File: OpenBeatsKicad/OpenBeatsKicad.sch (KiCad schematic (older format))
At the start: 30 parts

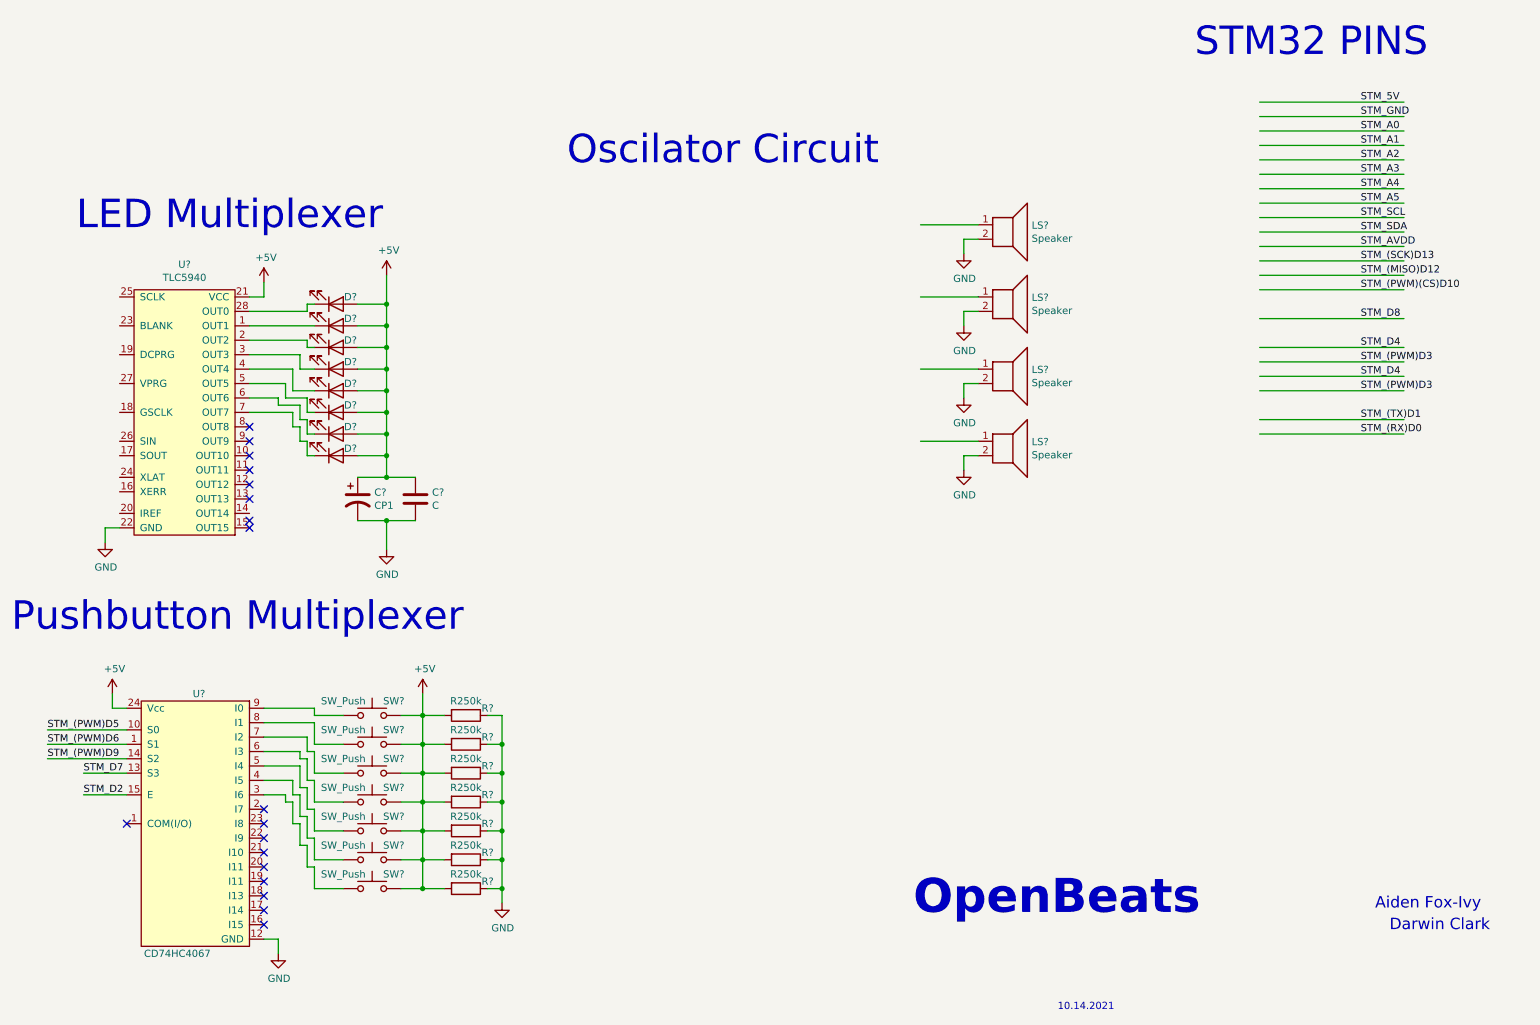
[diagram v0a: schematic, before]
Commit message: :sparkles: Connected all STM Pins, Finished Oscilator, and fixed naming conventions for passive components
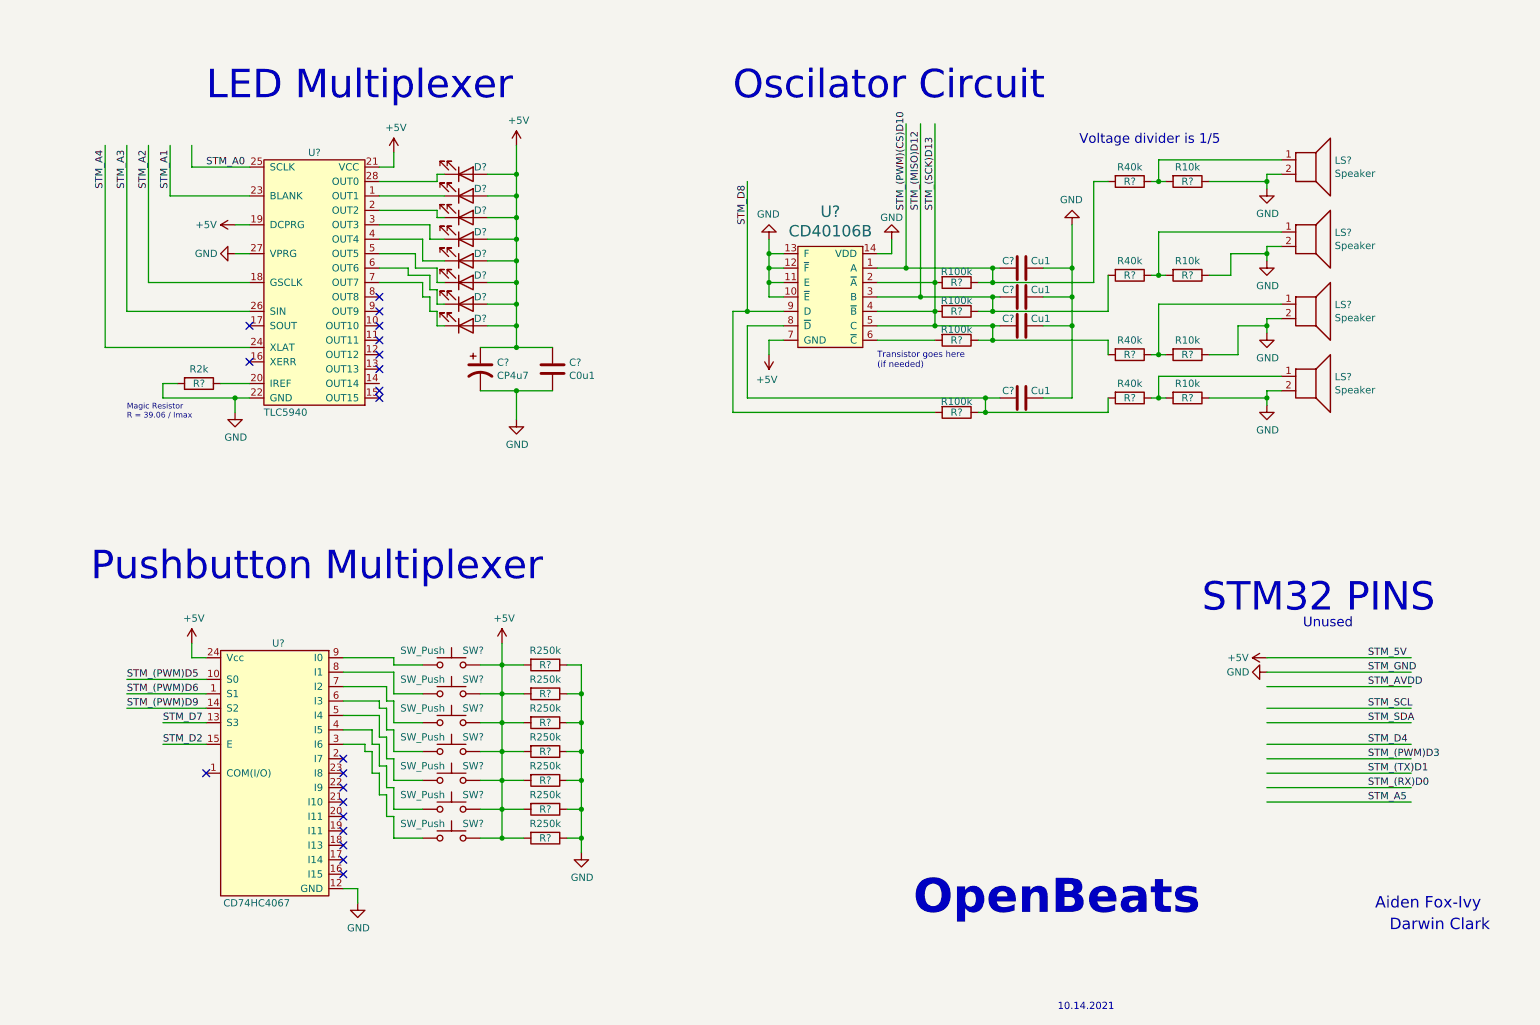
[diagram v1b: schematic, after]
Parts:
- added C? (x4): Cu1, symbol Device:C
- added R? (x4): R100k, symbol Device:R
- added R? (x4): R40k, symbol Device:R
- added R? (x4): R10k, symbol Device:R
- added R?: R2k, symbol Device:R
- added U?: CD40106B, symbol OpenBeatsSymbolLibrary:CD40106B
- C?: value C -> C0u1
- C?: value CP1 -> CP4u7
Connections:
- wire segments 180 -> 272
- no-connect marks 18 -> 20
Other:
- note added: "Magic Resistor\nR = 39.06 / Imax"
- note added: "Transistor goes here \n(if needed)"
- note added: "Unused"
- note added: "Voltage divider is 1/5\n"
- moved on the sheet: C?, D?, LS?, R?, SW?, U?
